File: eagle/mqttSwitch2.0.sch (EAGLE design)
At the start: 18 parts, among them IC1 AMS117 3.3, K1 G5LE, T1 2N3904

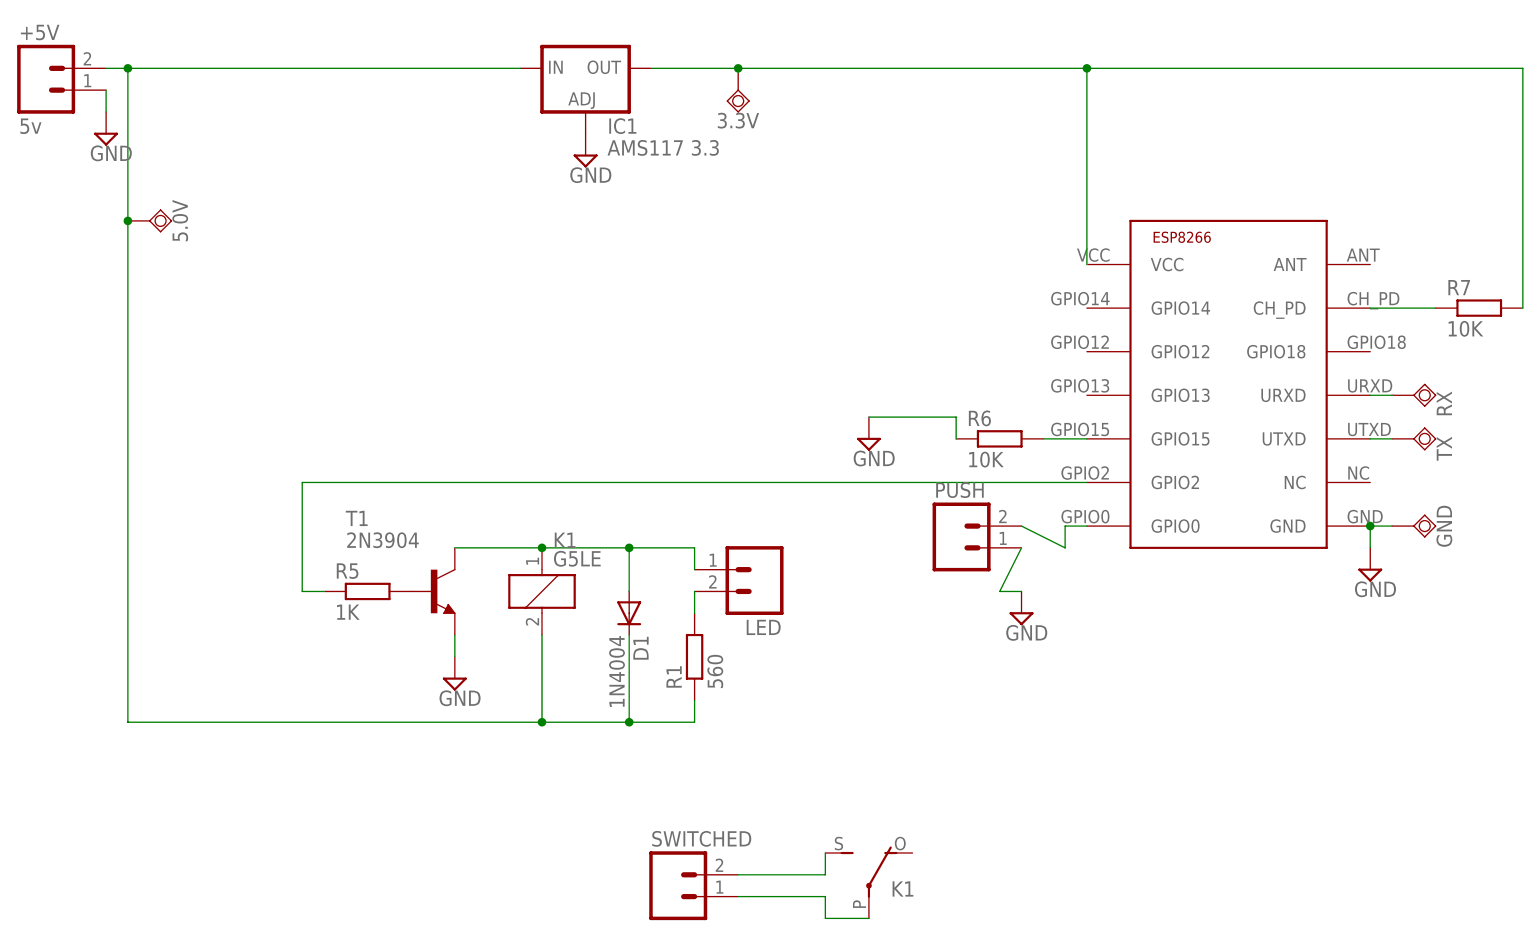
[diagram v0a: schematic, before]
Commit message: Updated to NPN, Started on KiCad
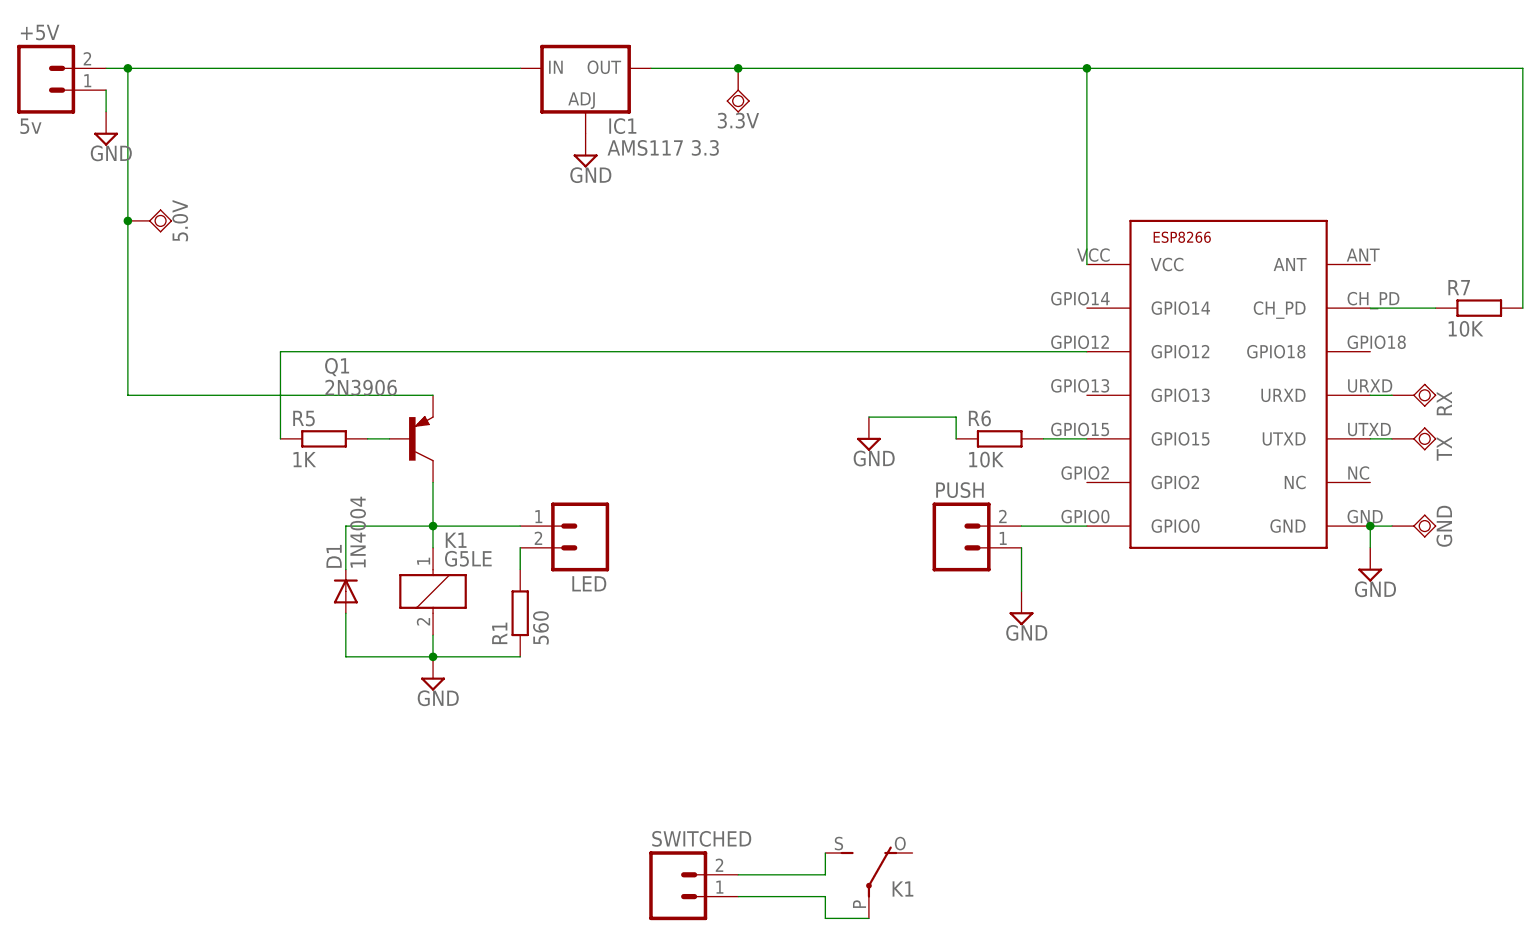
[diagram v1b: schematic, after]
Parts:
- removed T1: 2N3904, transistor:2N3904
- added Q1: 2N3906, transistor-pnp:2N3906
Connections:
- removed net N$12 (its old number): +5V.2, 5.0V.TP, D1.C, IC1.IN, K11.2, R1.1
- removed net N$4: R5.1, U$1.GPIO2
- new net N$13: R5.1, U$1.GPIO12
- new net N$8: D1.C, K11.1, LED.1, Q1.C
- net GND: now also D1.A, K11.2, R1.1; no longer T1.E
- net N$5: now also +5V.2, 5.0V.TP, IC1.IN, Q1.E; no longer D1.A, K11.1, LED.1, T1.C
- net N$6: now also Q1.B; no longer T1.B
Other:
- moved on the sheet: D1, K1, LED, R1, R5
